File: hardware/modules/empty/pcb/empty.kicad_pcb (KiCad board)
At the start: 2 copper layers, 25.5 x 32 mm, 5 parts

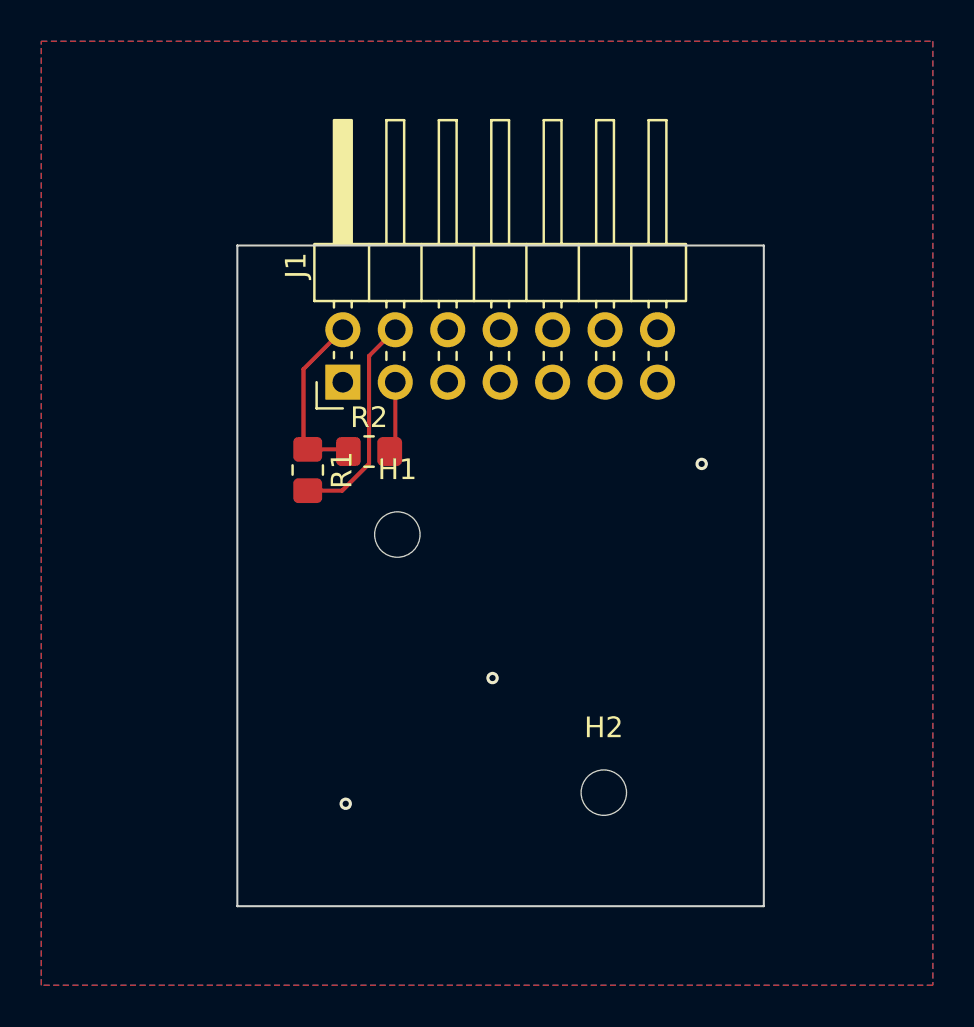
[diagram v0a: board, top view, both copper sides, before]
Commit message: added footprint with edge cuts for module
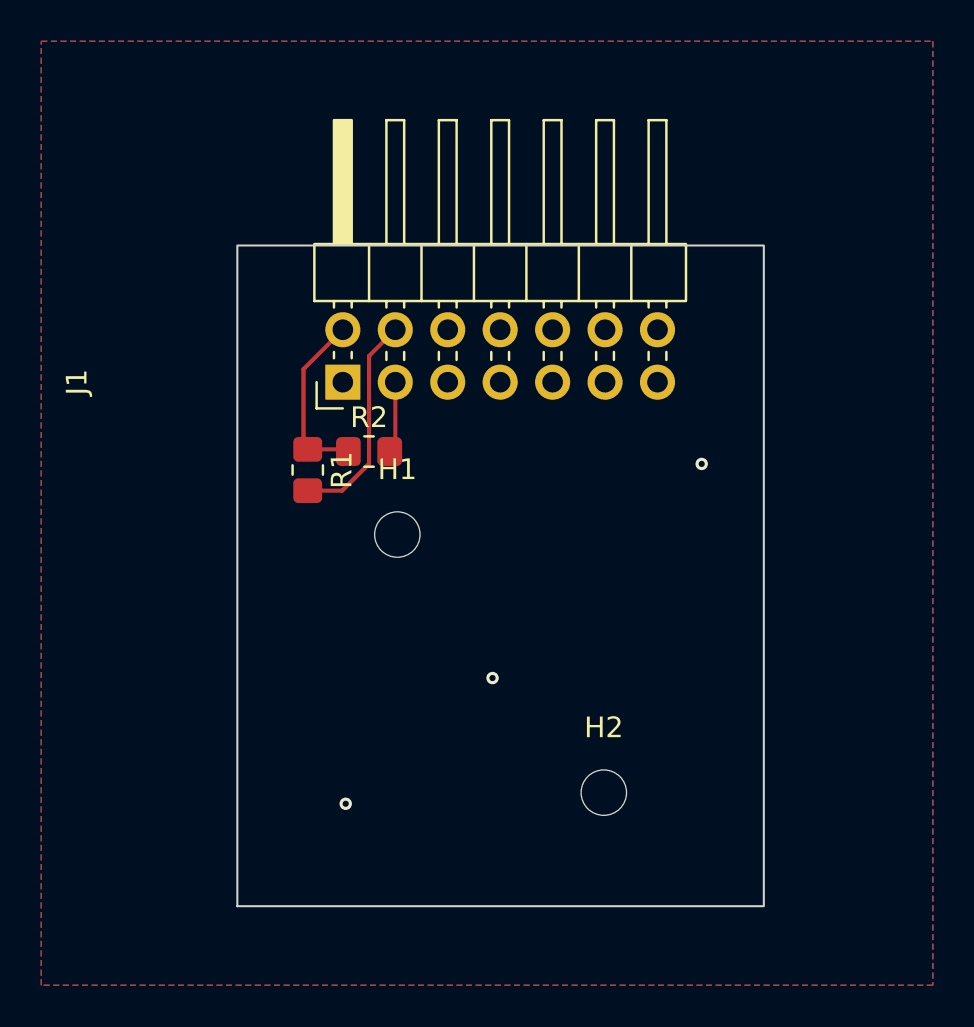
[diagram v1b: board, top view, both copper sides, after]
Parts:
- J1: footprint Connector_PinHeader_2.54mm:PinHeader_2x07_P2.54mm_Horizontal -> Hackxpansion:Male_Module
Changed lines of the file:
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@@
 		(capping no)
 		(filling no)
-		(zone_defaults)
 		(grid_origin 132.98 93.72)
 		(pcbplotparams
@@
 		)
 	)
-	(footprint "Connector_PinHeader_2.54mm:PinHeader_2x07_P2.54mm_Horizontal"
+	(footprint "Hackxpansion:Male_Module"
 		(layer "F.Cu")
 		(at 132.98 93.72 90)
-		(descr "Through hole angled pin header, 2x07, 2.54mm pitch, 6mm pin length, double rows")
-		(tags "Through hole angled pin header THT 2x07 2.54mm double row")
 		(property "Reference" "J1"
-			(at 5.655 -2.27 90)
-			(layer "F.SilkS")
+			(at 0 -12.88 90)
+			(unlocked yes)
+			(layer "F.SilkS")
+			(effects
+				(font
+					(size 1 1)
+					(thickness 0.1)
+				)
+			)
+		)
+		(property "Value" "~"
+			(at 0 -11.38 90)
+			(unlocked yes)
+			(layer "F.Fab")
 			(effects
 				(font
@@
 			)
 		)
-		(property "Value" "~"
-			(at 5.655 17.51 90)
-			(layer "F.Fab")
+		(property "Datasheet" ""
+			(at 0 0 90)
+			(unlocked yes)
+			(layer "F.Fab")
+			(hide yes)
 			(effects
 				(font
@@
 			)
 		)
-		(property "Datasheet" ""
-			(at 0 0 90)
-			(layer "F.Fab")
-			(hide yes)
-			(effects
-				(font
-					(size 1.27 1.27)
-				)
-			)
-		)
 		(property "Description" ""
 			(at 0 0 90)
+			(unlocked yes)
 			(layer "F.Fab")
 			(hide yes)
 			(effects
 				(font
-					(size 1.27 1.27)
+					(size 1 1)
+					(thickness 0.15)
 				)
 			)
@@
 			)
 		)
-		(attr through_hole)
+		(attr smd)
 		(duplicate_pad_numbers_are_jumpers no)
 		(fp_line
 			(start -1.27 -1.27)
-			(end 0 -1.270001)
-			(stroke
-				(width 0.12)
-				(type solid)
-			)
-			(layer "F.SilkS")
-		)
-		(fp_line
-			(start 3.617357 -0.43)
+			(end 0 -1.27)
+			(stroke
+				(width 0.12)
+				(type solid)
+			)
+			(layer "F.SilkS")
+		)
+		(fp_line
+			(start 3.617358 -0.43)
 			(end 3.93 -0.43)
 			(stroke
@@
 		)
 		(fp_line
-			(start -1.270001 0)
+			(start -1.27 0)
 			(end -1.27 -1.27)
 			(stroke
@@
 		)
 		(fp_line
-			(start 3.617357 0.43)
+			(start 3.617358 0.43)
 			(end 3.93 0.43)
 			(stroke
@@
 		(fp_line
 			(start 12.69 2.97)
-			(end 6.69 2.970001)
+			(end 6.69 2.97)
+			(stroke
+				(width 0.12)
+				(type solid)
+			)
+			(layer "F.SilkS")
+		)
+		(fp_line
+			(start 3.617358 2.97)
+			(end 3.93 2.97)
 			(stroke
 				(width 0.12)
@@
 		)
 		(fp_line
-			(start 3.617358 2.970001)
-			(end 3.93 2.97)
-			(stroke
-				(width 0.12)
-				(type solid)
-			)
-			(layer "F.SilkS")
-		)
-		(fp_line
 			(start 3.93 3.81)
 			(end 6.69 3.81)
@@
 		)
 		(fp_line
-			(start 12.690001 4.65)
-			(end 12.69 5.509999)
+			(start 12.69 4.65)
+			(end 12.69 5.51)
 			(stroke
 				(width 0.12)
@@
 		(fp_line
 			(start 6.69 4.65)
-			(end 12.690001 4.65)
+			(end 12.69 4.65)
 			(stroke
 				(width 0.12)
@@
 		(fp_line
 			(start 1.077358 4.65)
-			(end 1.462643 4.65)
-			(stroke
-				(width 0.12)
-				(type solid)
-			)
-			(layer "F.SilkS")
-		)
-		(fp_line
-			(start 12.69 5.509999)
+			(end 1.462642 4.65)
+			(stroke
+				(width 0.12)
+				(type solid)
+			)
+			(layer "F.SilkS")
+		)
+		(fp_line
+			(start 12.69 5.51)
 			(end 6.69 5.51)
 			(stroke
@@
 		(fp_line
 			(start 1.077358 5.51)
-			(end 1.462642 5.509999)
+			(end 1.462642 5.51)
 			(stroke
 				(width 0.12)
@@
 		(fp_line
 			(start 3.93 6.35)
-			(end 6.689999 6.35)
+			(end 6.69 6.35)
 			(stroke
 				(width 0.12)
@@
 		(fp_line
 			(start 12.69 7.19)
-			(end 12.69 8.050001)
+			(end 12.69 8.05)
 			(stroke
 				(width 0.12)
@@
 		)
 		(fp_line
+			(start 12.69 8.05)
+			(end 6.69 8.05)
+			(stroke
+				(width 0.12)
+				(type solid)
+			)
+			(layer "F.SilkS")
+		)
+		(fp_line
 			(start 3.617358 8.05)
 			(end 3.93 8.05)
@@
 		(fp_line
 			(start 1.077358 8.05)
-			(end 1.462642 8.050001)
-			(stroke
-				(width 0.12)
-				(type solid)
-			)
-			(layer "F.SilkS")
-		)
-		(fp_line
-			(start 12.69 8.050001)
-			(end 6.69 8.05)
+			(end 1.462642 8.05)
 			(stroke
 				(width 0.12)
@@
 		)
 		(fp_line
-			(start 6.689999 9.73)
+			(start 6.69 9.73)
 			(end 12.69 9.73)
 			(stroke
@@
 		)
 		(fp_line
-			(start 3.617357 9.73)
+			(start 3.617358 9.73)
 			(end 3.93 9.73)
 			(stroke
@@
 		(fp_line
 			(start 12.69 13.13)
-			(end 6.689999 13.13)
-			(stroke
-				(width 0.12)
-				(type solid)
-			)
-			(layer "F.SilkS")
-		)
-		(fp_line
-			(start 3.617357 13.13)
+			(end 6.69 13.13)
+			(stroke
+				(width 0.12)
+				(type solid)
+			)
+			(layer "F.SilkS")
+		)
+		(fp_line
+			(start 3.617358 13.13)
 			(end 3.93 13.13)
 			(stroke
@@
 		)
 		(fp_line
-			(start 12.69 14.809999)
+			(start 12.69 14.81)
 			(end 12.69 15.67)
 			(stroke
@@
 		(fp_line
 			(start 6.69 14.81)
-			(end 12.69 14.809999)
+			(end 12.69 14.81)
 			(stroke
 				(width 0.12)
@@
 		(fp_line
 			(start 1.077358 14.81)
-			(end 1.462643 14.81)
+			(end 1.462642 14.81)
 			(stroke
 				(width 0.12)
@@
 			(layer "F.SilkS")
 		)
-		(fp_poly
-			(pts
-				(xy 3.93 -1.38) (xy 3.93 16.62) (xy 6.69 16.62) (xy 6.69 -1.38)
-			)
+		(fp_rect
+			(start 3.93 -1.38)
+			(end 6.69 16.62)
 			(stroke
 				(width 0.12)
@@
 			(layer "F.SilkS")
 		)
-		(fp_poly
-			(pts
-				(xy 6.689999 -0.43) (xy 6.689999 0.43) (xy 12.69 0.43) (xy 12.69 -0.43)
-			)
+		(fp_rect
+			(start 6.69 -0.43)
+			(end 12.69 0.43)
 			(stroke
 				(width 0.12)
@@
 			(layer "F.SilkS")
 		)
-		(fp_poly
-			(pts
-				(xy -1.77 -1.77) (xy -1.77 17.019999) (xy 13.09 17.02) (xy 13.09 -1.77)
-			)
+		(fp_rect
+			(start -25.38 -4.11)
+			(end -1.88 19.39)
+			(stroke
+				(width 0.1)
+				(type solid)
+			)
+			(fill no)
+			(layer "Dwgs.User")
+		)
+		(fp_rect
+			(start -25.38 -5.11)
+			(end 6.62 20.39)
+			(radius 1)
+			(stroke
+				(width 0.1)
+				(type solid)
+			)
+			(fill no)
+			(layer "Edge.Cuts")
+		)
+		(fp_rect
+			(start -1.77 -1.77)
+			(end 13.09 17.02)
 			(stroke
 				(width 0.05)
@@
 		(fp_line
 			(start 6.58 -1.27)
-			(end 6.580001 16.51)
+			(end 6.58 16.51)
 			(stroke
 				(width 0.1)
@@
 		)
 		(fp_line
-			(start 6.580001 2.22)
+			(start 6.58 2.22)
 			(end 12.58 2.22)
 			(stroke
@@
 		(fp_line
 			(start -0.32 2.22)
-			(end 4.039999 2.22)
+			(end 4.04 2.22)
 			(stroke
 				(width 0.1)
@@
 		)
 		(fp_line
-			(start 6.580001 10.48)
+			(start 6.58 10.48)
 			(end 12.58 10.48)
 			(stroke
@@
 		(fp_line
 			(start -0.32 10.48)
-			(end 4.039999 10.48)
+			(end 4.04 10.48)
 			(stroke
 				(width 0.1)
@@
 		)
 		(fp_line
-			(start 6.580001 12.38)
+			(start 6.58 12.38)
 			(end 12.58 12.38)
 			(stroke
@@
 		(fp_line
 			(start -0.32 12.38)
-			(end 4.039999 12.38)
+			(end 4.04 12.38)
 			(stroke
 				(width 0.1)
@@
 		)
 		(fp_line
-			(start 6.580001 16.51)
-			(end 4.039999 16.51)
-			(stroke
-				(width 0.1)
-				(type solid)
-			)
-			(layer "F.Fab")
-		)
-		(fp_line
-			(start 4.039999 16.51)
+			(start 6.58 16.51)
+			(end 4.04 16.51)
+			(stroke
+				(width 0.1)
+				(type solid)
+			)
+			(layer "F.Fab")
+		)
+		(fp_line
+			(start 4.04 16.51)
 			(end 4.04 -0.635)
 			(stroke
@@
 		)
 		(fp_text user "${REFERENCE}"
-			(at 5.31 7.62 0)
+			(at 5.31 7.62 180)
 			(layer "F.Fab")
 			(effects
@@
 		)
 		(pad "5" thru_hole circle
-			(at 0 5.079999 90)
+			(at 0 5.08 90)
 			(size 1.7 1.7)
 			(drill 1)
@@
 		)
 		(embedded_fonts no)
-		(model "${KICAD10_3DMODEL_DIR}/Connector_PinHeader_2.54mm.3dshapes/PinHeader_2x07_P2.54mm_Horizontal.step"
-			(offset
-				(xyz 0 0 0)
-			)
-			(scale
-				(xyz 1 1 1)
-			)
-			(rotate
-				(xyz 0 0 0)
-			)
-		)
 	)
 	(footprint "Resistor_SMD:R_0805_2012Metric_Pad1.20x1.40mm_HandSolder"
@@
 		(embedded_fonts no)
 	)
-	(gr_rect
-		(start 128.87 95.6)
-		(end 152.37 119.1)
-		(stroke
-			(width 0.1)
-			(type solid)
-		)
-		(fill no)
-		(layer "Dwgs.User")
-	)
-	(gr_rect
-		(start 127.87 87.1)
-		(end 153.37 119.1)
-		(radius 1)
-		(stroke
-			(width 0.1)
-			(type solid)
-		)
-		(fill no)
-		(layer "Edge.Cuts")
-	)
 	(via
